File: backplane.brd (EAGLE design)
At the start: 153.7 x 128.3 mm, 45 parts, among them J1 L717HDE15PD4CH4R, J10 5013310807, J11 5013310807, J12 5013310807, J13 5013310807, J14 5013311007, J15 5013311007, J16 5013311007, J17 5013311007, J18 5013311007, J19 5013311007, J2 1054301102, J20 5013311007, J21 5013311007, J22 5013311007, J23 5013311007, J24 SEAM-40-03.0-S-06-2-A-K-TR, J25 5055670271, J3 5011902017, J4 5013310807, J5 5013310807, J6 5013310807, J7 5013310807, J8 5013310807, J9 5013310807, U1 AM26LV32EIPWR, U10 AM26LV32EIPWR, U2 AM26LV32EIPWR, U3 AM26LV32EIPWR, U4 AM26LV32EIPWR, U5 AM26LV32EIPWR, U6 AM26LV32EIPWR, U7 AM26LV32EIPWR, U8 AM26LV32EIPWR, U9 AM26LV32EIPWR

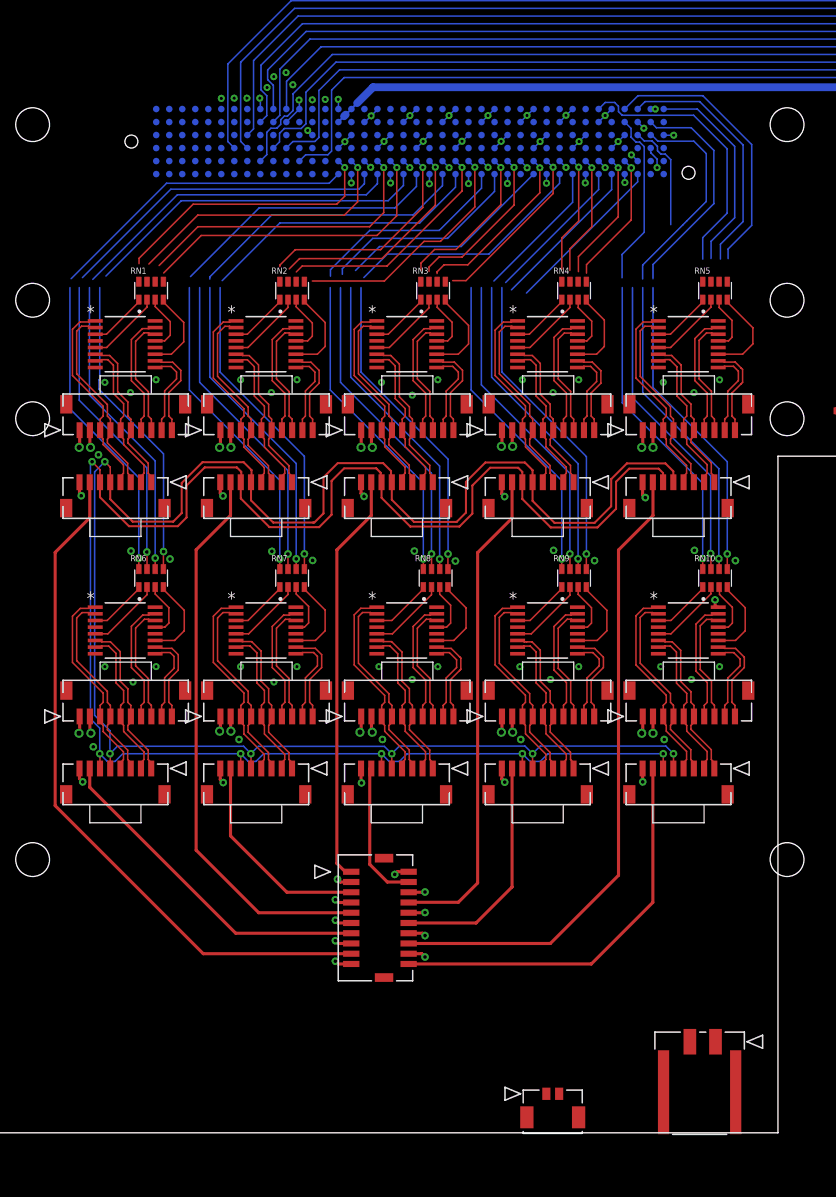
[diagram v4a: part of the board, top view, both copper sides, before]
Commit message: Routed power to AMC/encoder connectors and drivers
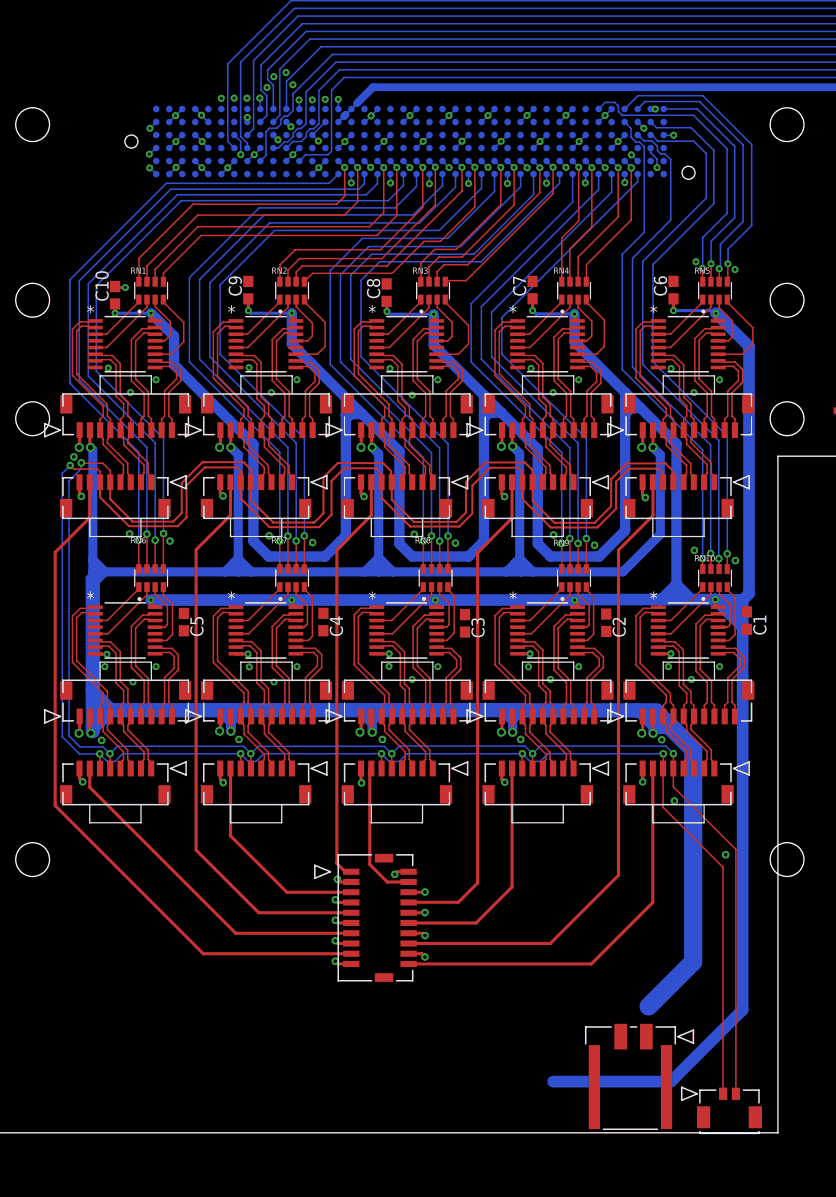
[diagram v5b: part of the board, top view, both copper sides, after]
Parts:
- added C1, C10, C2, C3, C4, C5, C6, C7, C8, C9: (no value), rcl:C0603
- moved J25 17.2 mm to (70.6, 3.81)
- moved J2 6.77 mm to (63.1, 9.39)
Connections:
- removed net N$1: RN9.5
- removed net N$10: RN10.7
- removed net N$11: RN10.8
- removed net N$12: RN8.7
- removed net N$14: RN8.8
- removed net N$15: RN7.5
- removed net N$16: RN7.6
- removed net N$17: RN7.7
- removed net N$18: RN7.8
- removed net N$19: RN6.5
- removed net N$2: RN9.6
- removed net N$20: RN6.6
- removed net N$21: RN6.7
- removed net N$22: RN6.8
- removed net N$24: RN5.5
- removed net N$25: RN5.6
- removed net N$26: RN5.7
- removed net N$27: RN5.8
- removed net N$28: RN4.5
- removed net N$29: RN4.6
- removed net N$3: RN9.7
- removed net N$31: RN4.7
- removed net N$32: RN4.8
- removed net N$33: RN3.5
- removed net N$34: RN3.6
- removed net N$35: RN3.7
- removed net N$36: RN3.8
- removed net N$38: RN2.5
- removed net N$39: RN2.6
- removed net N$40: RN2.7
- removed net N$41: RN2.8
- removed net N$42: RN1.5
- removed net N$43: RN1.6
- removed net N$45: RN1.7
- removed net N$46: RN1.8
- removed net N$5: RN9.8
- removed net N$6: RN8.5
- removed net N$7: RN8.6
- removed net N$8: RN10.5
- removed net N$9: RN10.6
- net 3V3: now also C1.1, C10.1, C2.1, C3.1, C4.1, C5.1, C6.1, C7.1, C8.1, C9.1
- net DIO0: now also RN9.5
- net DIO1: now also RN9.6
- net DIO10: now also RN7.7
- net DIO11: now also RN7.8
- net DIO12: now also RN6.5
- net DIO13: now also RN6.6
- net DIO14: now also RN6.7
- net DIO15: now also RN6.8
- net DIO16: now also RN10.6
- net DIO17: now also RN10.7
- net DIO2: now also RN9.7
- net DIO3: now also RN9.8
- net DIO32: now also RN4.5
- net DIO33: now also RN4.6
- net DIO34: now also RN4.7
- net DIO35: now also RN4.8
- net DIO36: now also RN3.5
- net DIO37: now also RN3.6
- net DIO38: now also RN3.7
- net DIO39: now also RN3.8
- net DIO4: now also RN8.5
- net DIO40: now also RN2.5
- net DIO41: now also RN2.6
- net DIO42: now also RN2.7
- net DIO43: now also RN2.8
- net DIO44: now also RN1.5
- net DIO45: now also RN1.6
- net DIO46: now also RN1.7
- net DIO47: now also RN1.8
- net DIO48: now also RN10.5
- net DIO49: now also RN10.8
- net DIO5: now also RN8.6
- net DIO6: now also RN8.7
- net DIO7: now also RN8.8
- net DIO8: now also RN7.5
- net DIO80: now also RN5.7
- net DIO81: now also RN5.6
- net DIO82: now also RN5.5
- net DIO83: now also RN5.8
- net DIO9: now also RN7.6
- net ESTP+: now also J25.2
- net ESTP-: now also J25.1
- net GND: now also C1.2, C10.2, C2.2, C3.2, C4.2, C5.2, C6.2, C7.2, C8.2, C9.2, J25.3, J25.4
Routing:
- net 3V3: track 0.96 -> 395.3 mm, vias 1 -> 15
- net 5V: track 16.3 -> 287.0 mm
- net DIO6: track 0.00 -> 54.8 mm, vias 0 -> 1
- net DIO8: track 20.1 -> 61.9 mm, vias 0 -> 1
- net ESTP+: track 185.1 -> 223.7 mm
- net DIO17: track 10.8 -> 49.2 mm, vias 0 -> 1
- net ESTP-: track 182.8 -> 221.1 mm
- net DIO5: track 21.3 -> 55.4 mm, vias 0 -> 1
- net DIO7: track 20.2 -> 53.8 mm, vias 0 -> 1
- net DIO10: track 27.7 -> 60.5 mm, vias 0 -> 1
- net DIO9: track 27.8 -> 60.6 mm, vias 0 -> 1
- net DIO3: track 13.6 -> 46.3 mm, vias 0 -> 1
- net DIO2: track 14.3 -> 46.9 mm, vias 0 -> 1
- net DIO11: track 26.9 -> 59.2 mm, vias 0 -> 1
- net DIO4: track 23.8 -> 55.9 mm, vias 0 -> 1
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- added copper zone on layer 15, net GND
- removed copper zone on layer 15, net 5V
- removed copper zone on layer 15, net 5V_SBRIO

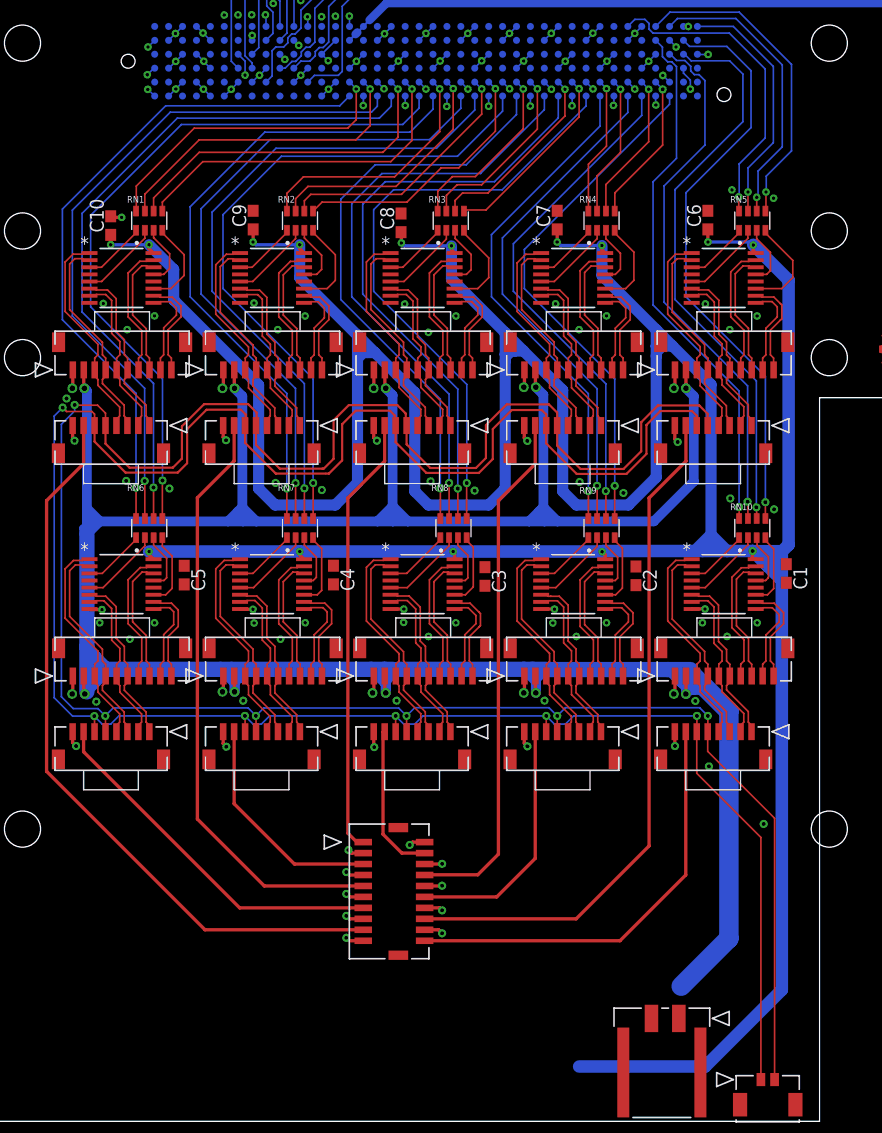
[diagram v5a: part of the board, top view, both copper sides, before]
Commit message: added bypass caps and routed G pins on drivers
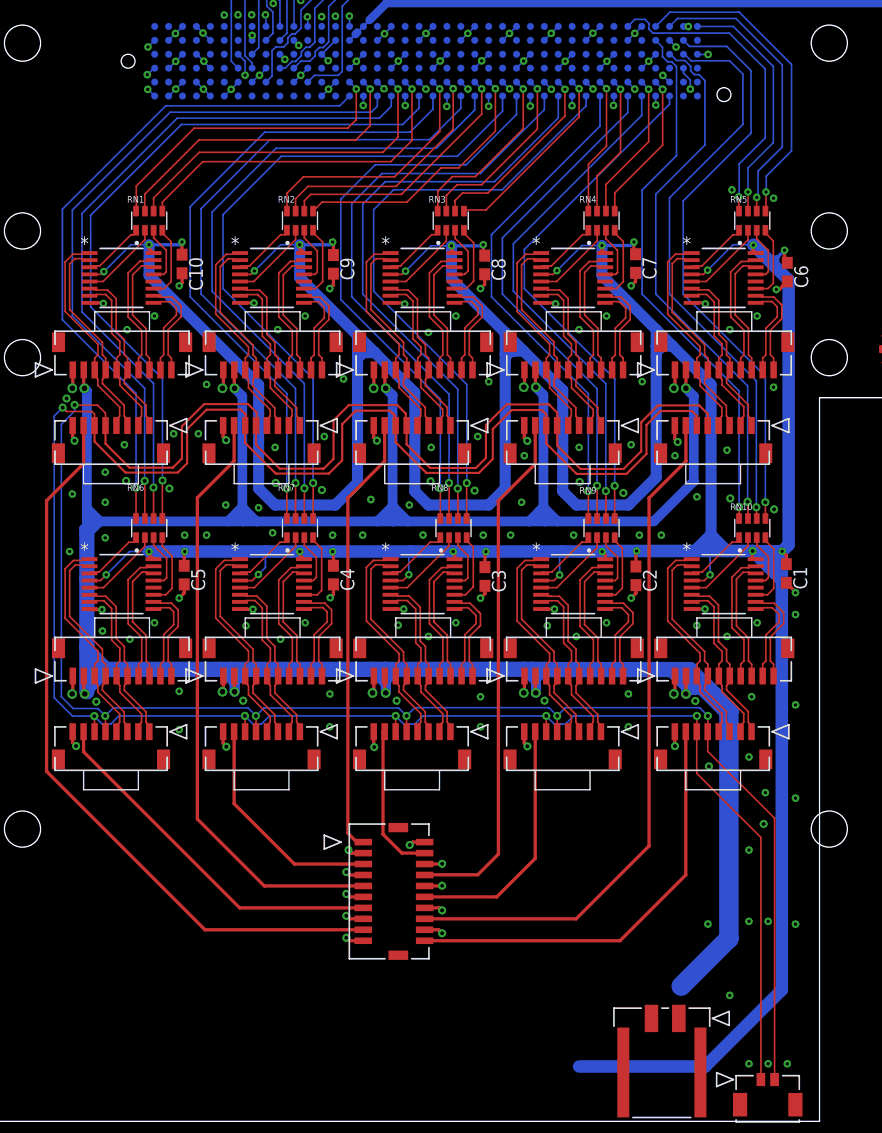
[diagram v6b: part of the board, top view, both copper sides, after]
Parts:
- moved C6 8.67 mm to (73.0, 77.5), turned to 270 degrees
- moved C8 8.54 mm to (45.4, 78.2), turned to 270 degrees
- moved C9 8.37 mm to (31.6, 78.2), turned to 270 degrees
- moved C7 8.18 mm to (59.1, 78.3), turned to 270 degrees
- moved C10 7.40 mm to (17.8, 78.2), turned to 270 degrees
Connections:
- removed net N$108: U4.4
- removed net N$124: U3.4
- removed net N$13: U10.4
- removed net N$140: U2.4
- removed net N$156: U1.4
- removed net N$30: U9.4
- removed net N$44: U8.4
- removed net N$60: U7.4
- removed net N$76: U6.4
- removed net N$92: U5.4
- net 3V3: now also U1.4, U10.4, U2.4, U3.4, U4.4, U5.4, U6.4, U7.4, U8.4, U9.4
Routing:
- net 3V3: track 395.3 -> 454.4 mm, vias 15 -> 30
- net GND: track 99.5 -> 118.5 mm, vias 149 -> 220
- net A_M2: track 9.16 -> 6.95 mm
- net A_M6: track 8.79 -> 7.04 mm
- net A_M8: track 8.58 -> 7.02 mm
- net A_M10: track 8.24 -> 6.90 mm
- net A_M4: track 8.24 -> 6.94 mm
- net DIO49: track 48.8 -> 49.6 mm
- net DIO17: track 49.2 -> 49.8 mm
